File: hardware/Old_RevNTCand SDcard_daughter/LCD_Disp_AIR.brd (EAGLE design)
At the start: 57.8 x 32.4 mm, 11 parts

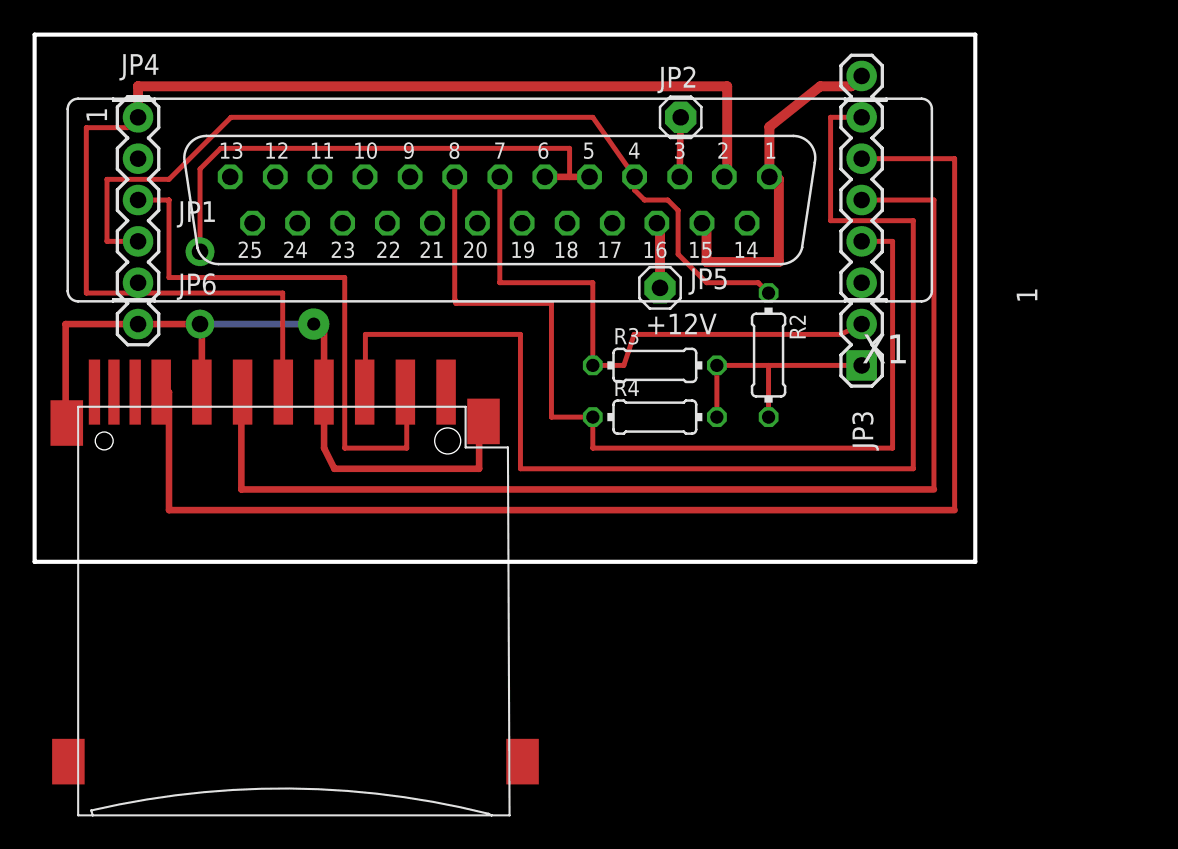
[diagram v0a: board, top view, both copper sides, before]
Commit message: added schematic for use as solder controller
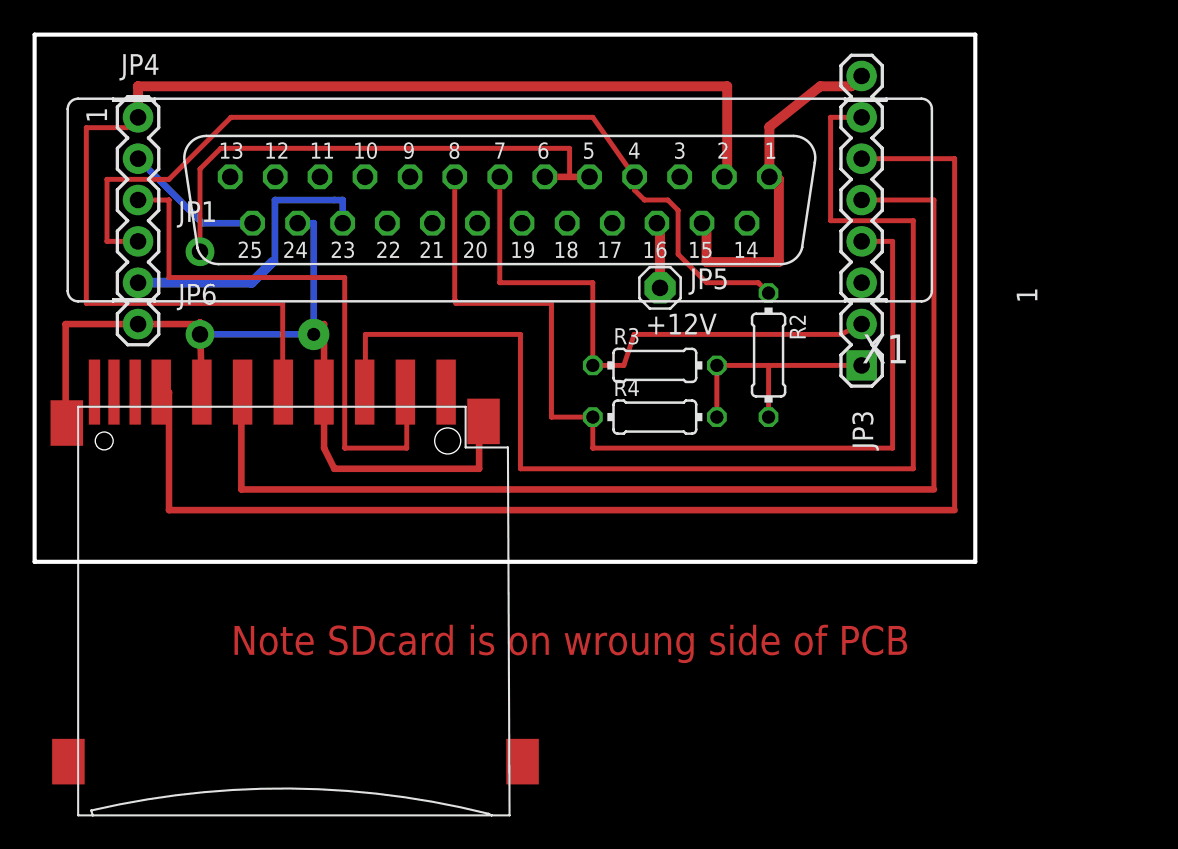
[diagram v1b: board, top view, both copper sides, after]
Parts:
- removed JP2: (no value), adafruit:1X01
- moved JP6 0.63 mm to (12.1, 27.9)
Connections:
- removed net SERVO: JP2.1, X1.3
- new net N$5: JP4.5, X1.23
- new net N$6: JP4.2, X1.25
- net GND: now also X1.24
- net N$4: no longer X1.1
- net VDD: no longer X1.2
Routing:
- net N$5: track 0.00 -> 18.3 mm
- net GND: track 42.9 -> 51.7 mm
- net N$6: track 0.00 -> 8.67 mm
- net SERVO: track 3.66 -> 0.00 mm
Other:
- board text added: "Note SDcard is on wroung side of PCB"
